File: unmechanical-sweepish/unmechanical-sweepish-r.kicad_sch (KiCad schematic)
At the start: 82 parts, among them J3 M, Q1 AO3400A, U11 OPA340NA, U5 74HC4051

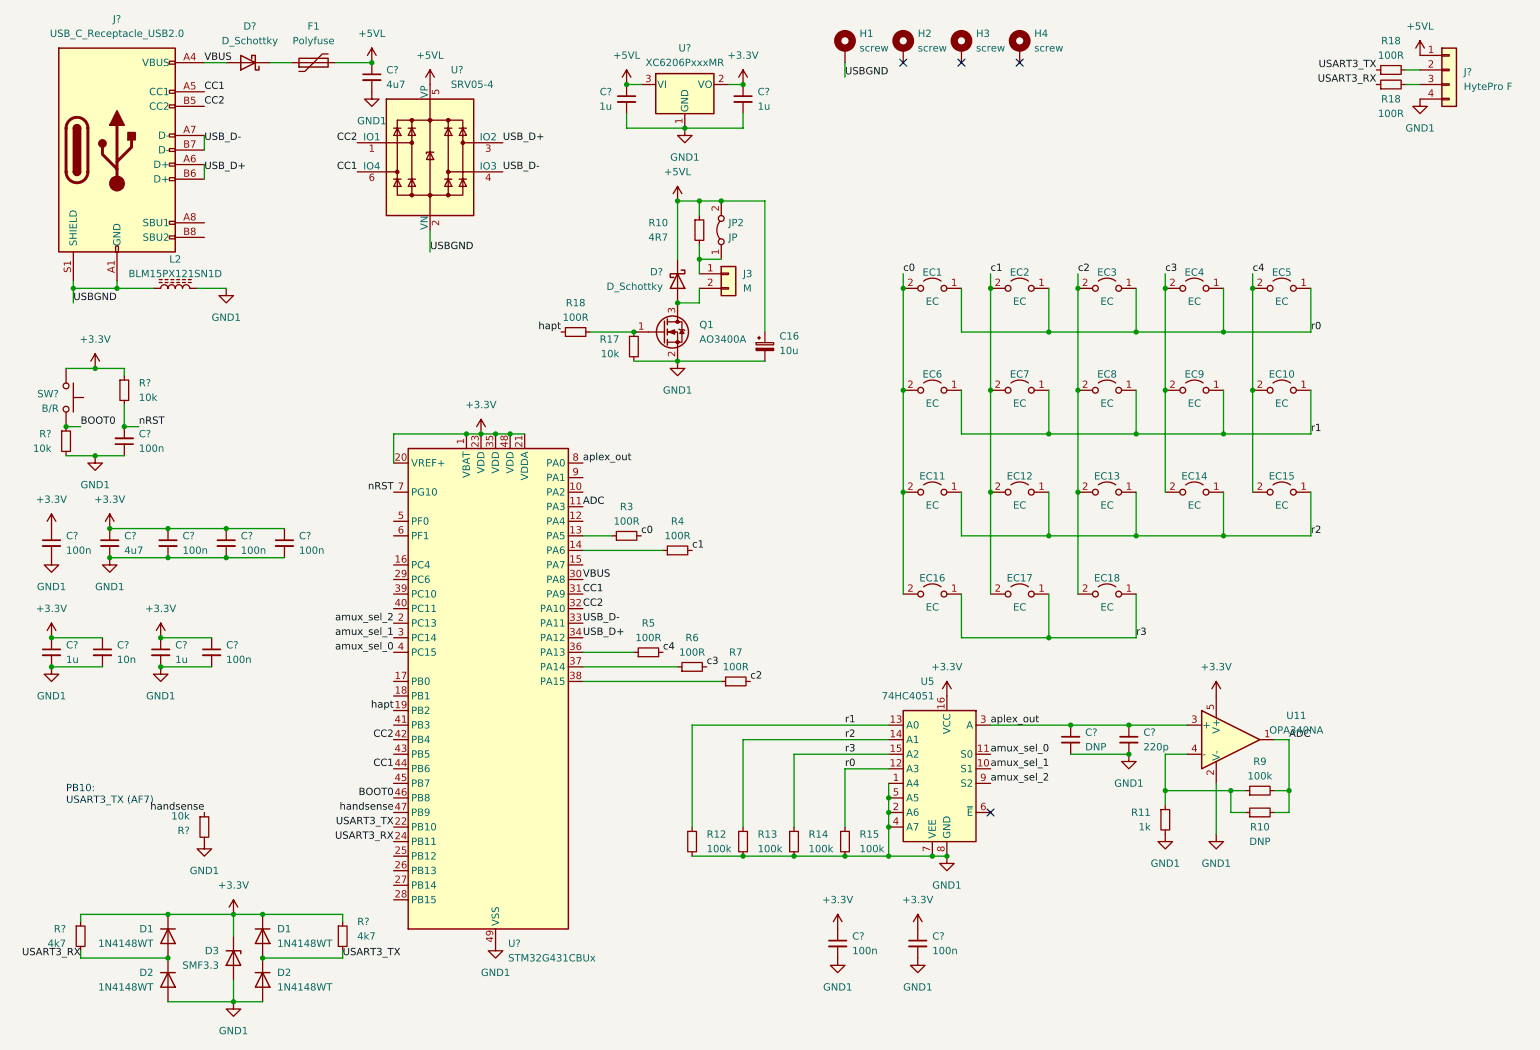
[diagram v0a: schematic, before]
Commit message: Migrate to v8
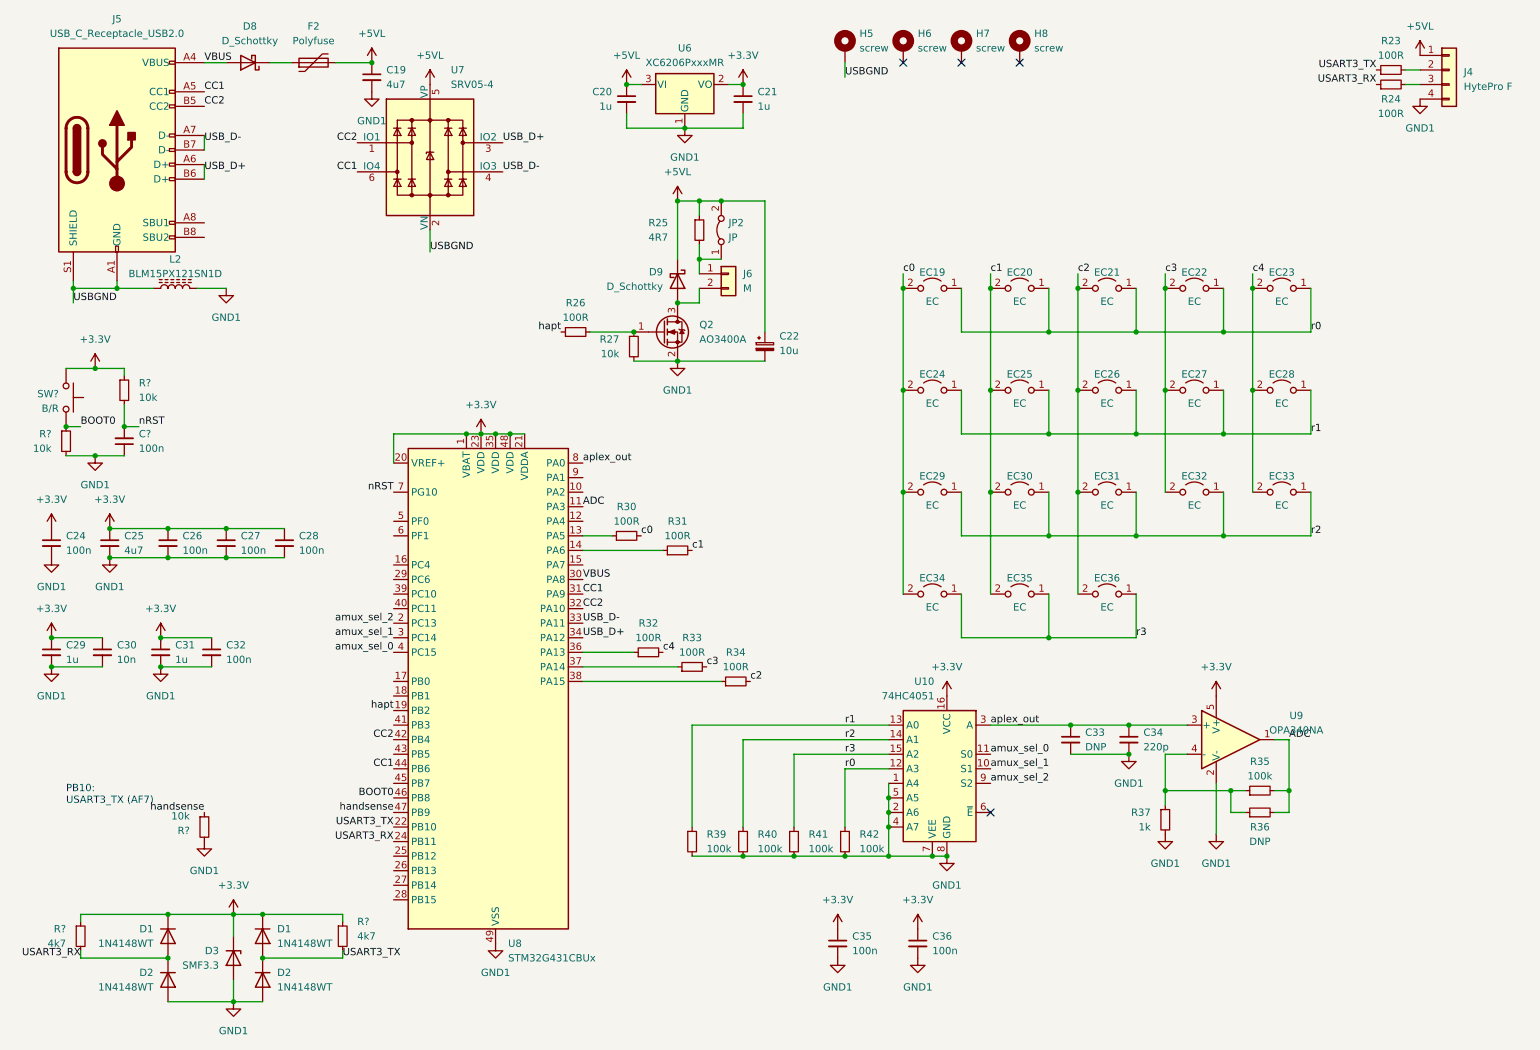
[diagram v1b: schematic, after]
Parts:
- L2: value BLM15PX121SN1D -> BLM15PX121SN1D
- gave numbers to parts that had none: 23
- renumbered C16 to C22, EC1 to EC19, EC2 to EC20, EC3 to EC21, EC4 to EC22, EC5 to EC23, EC6 to EC24, EC7 to EC25, EC8 to EC26, EC9 to EC27, EC10 to EC28, EC11 to EC29, EC12 to EC30, EC13 to EC31, EC14 to EC32, EC15 to EC33, EC16 to EC34, EC17 to EC35, EC18 to EC36, F1 to F2, H1 to H5, H2 to H6, H3 to H7, H4 to H8, J3 to J6, Q1 to Q2, R18 to R23, R18 to R24, R10 to R25, R18 to R26, R17 to R27, R3 to R30, R4 to R31, R5 to R32, R6 to R33, R7 to R34, R9 to R35, R10 to R36, R11 to R37, R12 to R39, R13 to R40, R14 to R41, R15 to R42, U5 to U10, U11 to U9

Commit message: Fix up for order
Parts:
- J4: footprint PCM_marbastlib-xp-various:CON_HytePro_M411P_Receptacle_1x04-P2.20mm_Horizontal_FlushMount -> Connector_PinHeader_2.54mm:PinHeader_1x04_P2.54mm_Vertical
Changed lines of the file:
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@@
 			)
 		)
-		(property "Footprint" "PCM_marbastlib-xp-various:CON_HytePro_M411P_Receptacle_1x04-P2.20mm_Horizontal_FlushMount"
+		(property "Footprint" "Connector_PinHeader_2.54mm:PinHeader_1x04_P2.54mm_Vertical"
 			(at 261.62 25.4 0)
 			(effects
